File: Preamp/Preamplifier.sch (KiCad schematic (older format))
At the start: 146 parts, among them J1 Conn_01x03_Male, J12 XLR3, J14 Conn_01x03, J15 Conn_01x02, J16 Conn_01x02, J17 Conn_01x02, J2 Conn_01x02_Male, J3 Conn_01x02_Male, J4 Conn_01x03_Male, J5 Conn_01x03_Male, J6 Conn_01x02_Male, J7 Conn_01x02, J8 Conn_01x05_Female, J9 Conn_01x03, Q3 2N3904, Q4 2N3906, Q5 BC549, SW1 SW_HPF, SW2 SW_SPDT, SW3 GND LIFT, SW4 SW_SPST, SW5 SW_HPFQ, U1 OPA2134, U2 NE5532, U4 NE5532, U5 TL072, U6 NE5532, U7 NE5532, U8 NE5532, U9 NE5532

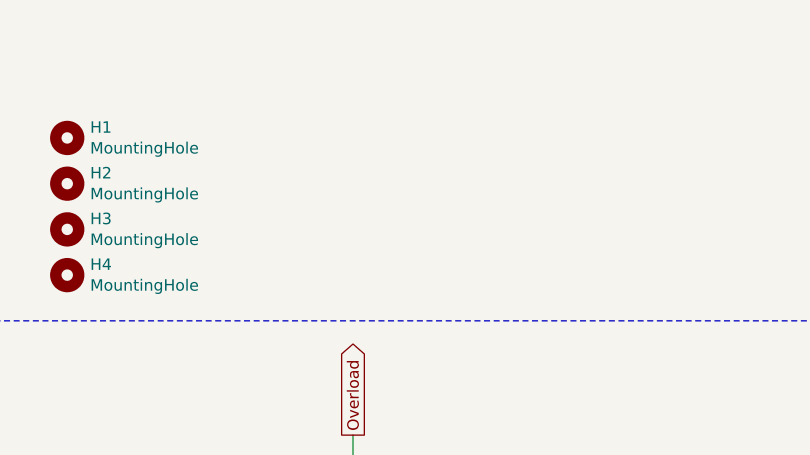
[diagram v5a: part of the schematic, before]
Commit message: Added bulk caps, started eq board layout
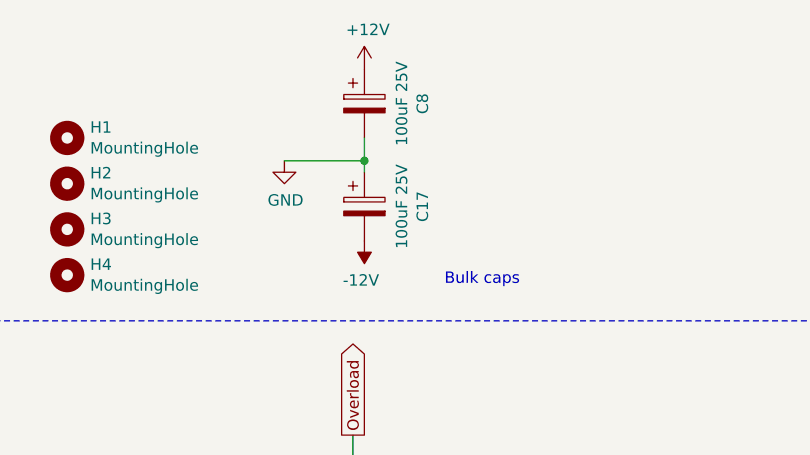
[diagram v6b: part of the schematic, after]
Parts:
- added C17, C8: 100uF 25V, Capacitor_THT:CP_Radial_D6.3mm_P2.50mm, symbol Device:CP
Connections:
- net +12V: now also C8.1
- net -12V: now also C17.2
- net GND: now also C17.1, C8.2
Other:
- note added: "Bulk caps"
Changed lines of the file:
@@
 Wire Wire Line
 	8500 11200 8200 11200
+$Comp
+L Device:CP C8
+U 1 1 5E5866B4
+P 5250 1000
+F 0 "C8" V 5505 1000 50  0000 C CNN
+F 1 "100uF 25V" V 5414 1000 50  0000 C CNN
+F 2 "Capacitor_THT:CP_Radial_D6.3mm_P2.50mm" H 5288 850 50  0001 C CNN
+F 3 "~" H 5250 1000 50  0001 C CNN
+	1    5250 1000
+	1    0    0    -1
+$EndComp
+$Comp
+L power:GND #PWR0122
+U 1 1 5E5877FA
+P 4900 1250
+F 0 "#PWR0122" H 4900 1000 50  0001 C CNN
+F 1 "GND" H 4905 1077 50  0000 C CNN
+F 2 "" H 4900 1250 50  0001 C CNN
+F 3 "" H 4900 1250 50  0001 C CNN
+	1    4900 1250
+	1    0    0    -1
+$EndComp
+Wire Wire Line
+	4900 1250 5250 1250
+Wire Wire Line
+	5250 1250 5250 1150
+Wire Wire Line
+	5250 1250 5250 1300
+Connection ~ 5250 1250
+Text Notes 5600 1800 0    50   ~ 0
+Bulk caps
+$Comp
+L power:+12V #PWR0123
+U 1 1 5E5EDA9F
+P 5250 850
+F 0 "#PWR0123" H 5250 700 50  0001 C CNN
+F 1 "+12V" H 5265 1023 50  0000 C CNN
+F 2 "" H 5250 850 50  0001 C CNN
+F 3 "" H 5250 850 50  0001 C CNN
+	1    5250 850
+	1    0    0    -1
+$EndComp
+$Comp
+L power:-12V #PWR0124
+U 1 1 5E5EDEE0
+P 5250 1600
+F 0 "#PWR0124" H 5250 1700 50  0001 C CNN
+F 1 "-12V" H 5265 1773 50  0000 C CNN
+F 2 "" H 5250 1600 50  0001 C CNN
+F 3 "" H 5250 1600 50  0001 C CNN
+	1    5250 1600
+	-1   0    0    1
+$EndComp
+$Comp
+L Device:CP C17
+U 1 1 5E58720B
+P 5250 1450
+F 0 "C17" V 5505 1450 50  0000 C CNN
+F 1 "100uF 25V" V 5414 1450 50  0000 C CNN
+F 2 "Capacitor_THT:CP_Radial_D6.3mm_P2.50mm" H 5288 1300 50  0001 C CNN
+F 3 "~" H 5250 1450 50  0001 C CNN
+	1    5250 1450
+	1    0    0    -1
+$EndComp
 $EndSCHEMATC
